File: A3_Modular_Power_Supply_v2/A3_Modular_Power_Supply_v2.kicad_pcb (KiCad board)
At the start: 2 copper layers, 70 x 40 mm, 74 parts, among them J1 JST-XH-S3B, J10 Conn_01x02_Pin, J11 Conn_01x02_Pin, J2 JST-XH-S3B, J3 JST-XH-S3B, J4 JST-XH-S3B, J5 JST-XH-S3B, J6 JST-XH-S3B, J7 JST-XH-S3B, Q1 CSD17522Q5A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

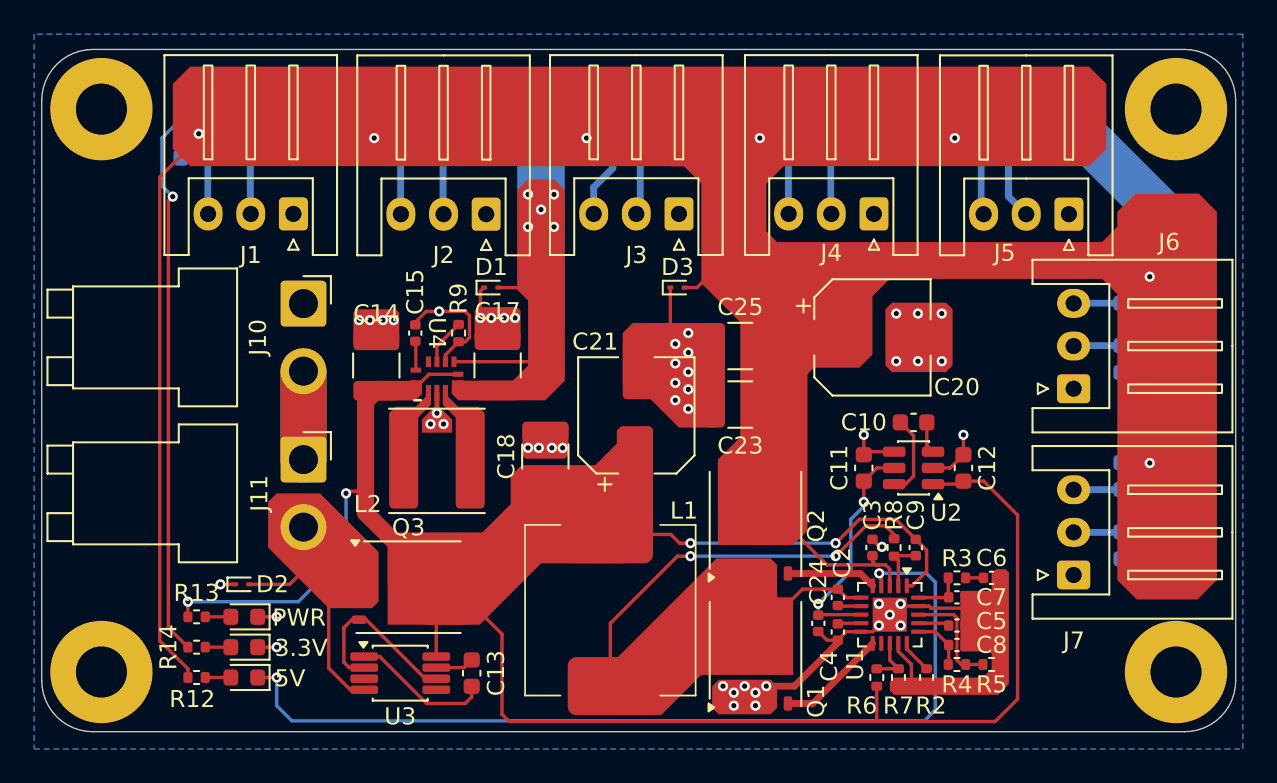
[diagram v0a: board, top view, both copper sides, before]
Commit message: Changed some capacitor package sizes
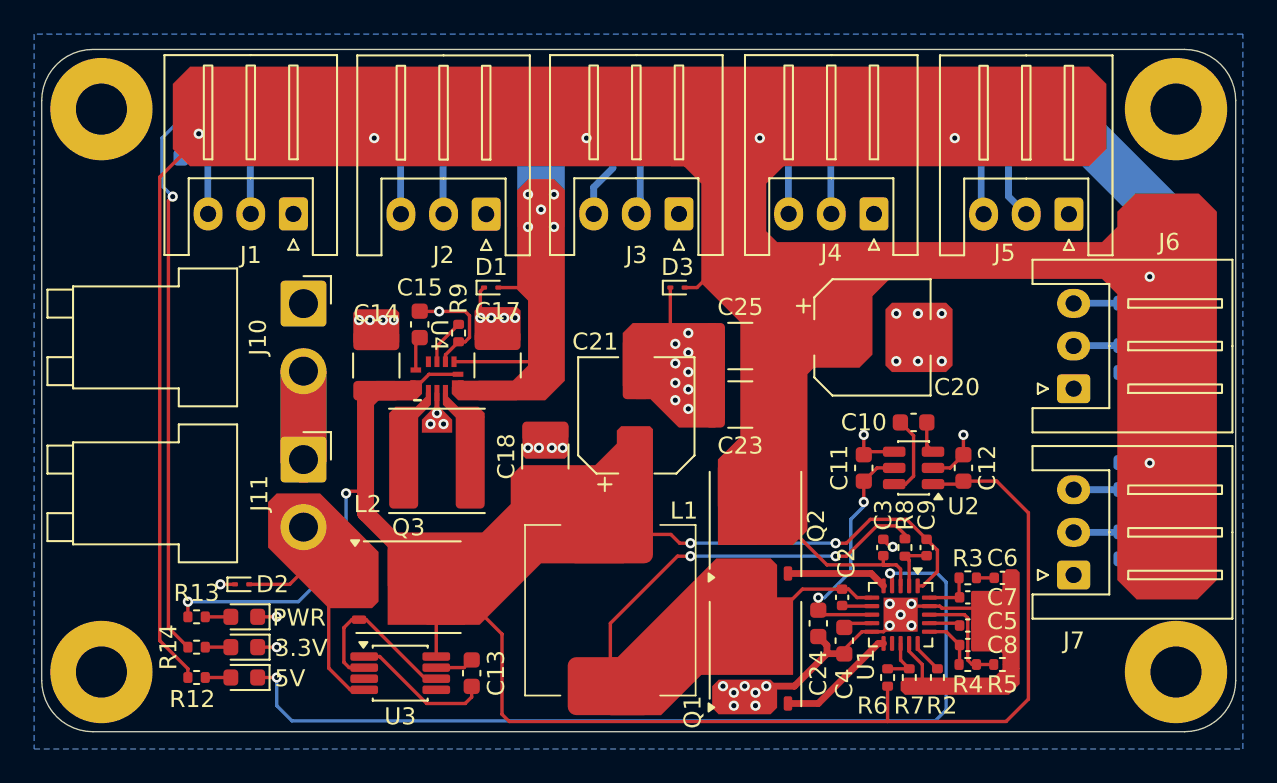
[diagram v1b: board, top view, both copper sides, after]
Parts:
- C15, C24, C4: footprint Capacitor_SMD:C_0402_1005Metric -> Capacitor_SMD:C_0603_1608Metric
- Q1, Q2, Q3: value CSD17522Q5A -> CSD17505Q5A
- moved C3 0.64 mm to (156.6, 90.8)
- moved C5 0.64 mm to (161.5, 95.4)
- moved C7 0.64 mm to (161.5, 93.7)
- moved C8 0.64 mm to (161.5, 96.5)
- moved R3 0.64 mm to (161.5, 92.6)
- moved R4 0.64 mm to (161.5, 97.7)
- moved R7 0.64 mm to (158.1, 98.4)
- moved C4 0.64 mm to (154.3, 96.3)
- moved C6 0.63 mm to (163.6, 92.6)
- moved C9 0.63 mm to (159.1, 90.8)
- moved R2 0.63 mm to (159.8, 98.4)
- moved R5 0.63 mm to (163.6, 97.7)
- moved R6 0.63 mm to (156.8, 98.4)
- moved R8 0.63 mm to (157.9, 90.8)
- moved U1 0.63 mm to (157.6, 94.7)
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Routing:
- net VBAT: track 117.2 -> 119.2 mm
- net Net-(Q1-D): track 30.7 -> 32.0 mm
- net /V_BIAS: track 13.6 -> 14.6 mm
- net Net-(U1-VCC): track 1.38 -> 2.06 mm
- net +5V: track 112.2 -> 112.9 mm
- net /PGOOD: track 53.8 -> 54.4 mm
- net Net-(Q1-G): track 6.43 -> 7.06 mm
- net Net-(Q2-G): track 5.27 -> 5.90 mm

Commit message: Connector labels, heatsink mounting
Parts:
- added REF**: MountingHole_2mm, MountingHole:MountingHole_2mm, F.Cu at (122.3, 98.2)
- added REF**: MountingHole_2mm, MountingHole:MountingHole_2mm, F.Cu at (167.3, 98.2)
- added REF**: MountingHole_2mm, MountingHole:MountingHole_2mm, F.Cu at (136.3, 80.2)
- moved D3 18.1 mm to (162.6, 76.6)
- moved C15 10.2 mm to (131.9, 87.6), turned to -90 degrees
- moved C14 9.42 mm to (135.2, 84.5), turned to 0 degrees
- moved R9 9.12 mm to (129.7, 87.1), turned to 90 degrees
- moved D2 9.04 mm to (126.9, 88.5), turned to 180 degrees
- moved C17 8.33 mm to (127.4, 85.2), turned to -90 degrees
- moved C18 7.04 mm to (143.8, 86.4), turned to 0 degrees
- moved L2 6.12 mm to (130.9, 79.6), turned to 180 degrees
- moved R12 5.26 mm to (115.6, 93.2), turned to 90 degrees
- moved D4 4.45 mm to (115.6, 95.8), turned to 90 degrees
- moved U4 3.59 mm to (130.9, 84.5), turned to -90 degrees
- moved R14 3.58 mm to (117.3, 93.2), turned to 90 degrees
- moved C21 3.43 mm to (142.1, 79.6)
- moved R13 3.25 mm to (119.1, 93.2), turned to 90 degrees
- moved D1 2.74 mm to (136.3, 76.2), turned to 180 degrees
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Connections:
- REF** pad 1: (no net) -> GND
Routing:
- net +5V: track 112.9 -> 63.7 mm
- net VBAT: track 119.2 -> 104.6 mm
- net /PGOOD: track 54.4 -> 60.5 mm
- net +3.3V: track 145.3 -> 144.1 mm, vias 6 -> 5
- net Net-(J2-Pin_3): track 2.69 -> 3.70 mm
- net GND: track 40.9 -> 40.1 mm, vias 49 -> 50
- net /BATT_IN: track 14.8 -> 15.4 mm
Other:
- board text added: "GND"
